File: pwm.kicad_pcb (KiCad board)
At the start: 2 copper layers, 10 parts, among them U501 LTC6992IS6-1

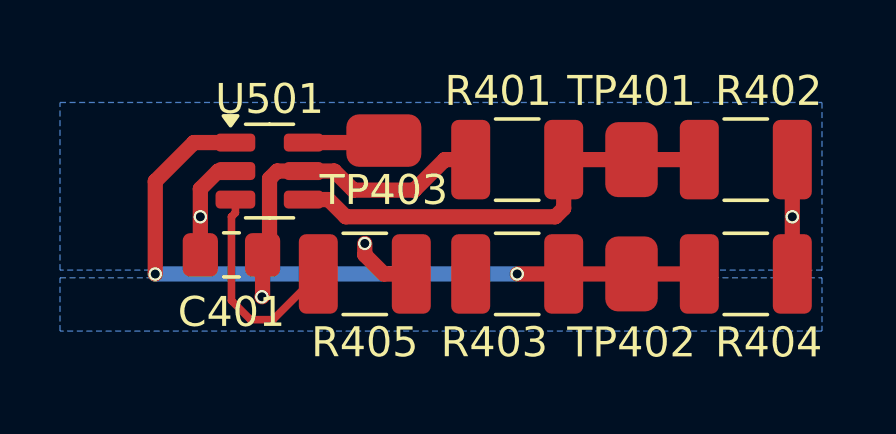
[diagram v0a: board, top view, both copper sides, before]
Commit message: enhance silk screen
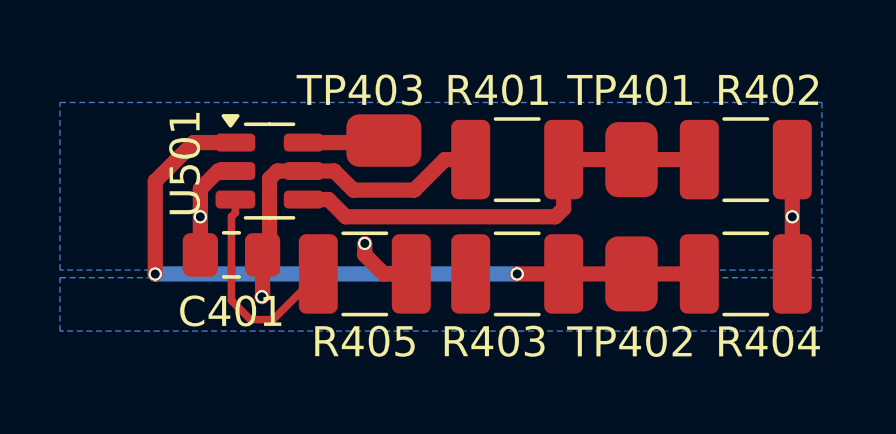
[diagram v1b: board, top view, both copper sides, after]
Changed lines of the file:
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@@
 		(tags "resistor")
 		(property "Reference" "TP403"
-			(at 0 -1.65 180)
+			(at 0.762 1.651 180)
 			(layer "F.SilkS")
 			(effects
@@
 		(tags "capacitor handsolder")
 		(property "Reference" "C401"
-			(at 0 1.905 360)
+			(at 0 1.905 0)
 			(layer "F.SilkS")
 			(effects
@@
 		)
 		(property "Value" "100n"
-			(at 0 1.68 360)
+			(at 0 1.68 0)
 			(layer "F.Fab")
 			(effects
@@
 		)
 		(fp_text user "${REFERENCE}"
-			(at 0 0 360)
+			(at 0 0 0)
 			(layer "F.Fab")
 			(effects
@@
 		)
 		(property "Value" "~"
-			(at 0 1.65 270)
+			(at 0 1.65 -90)
 			(layer "F.Fab")
 			(effects
@@
 		)
 		(fp_text user "${REFERENCE}"
-			(at 0 0 270)
+			(at 0 0 -90)
 			(layer "F.Fab")
 			(effects
@@
 		(tags "TSOT TO_SOT_SMD")
 		(property "Reference" "U501"
-			(at 0 -2.4 360)
+			(at -2.794 -0.254 90)
 			(layer "F.SilkS")
 			(effects
@@
 		)
 		(property "Value" "LTC6992IS6-1"
-			(at 2.365 6.21 360)
+			(at 2.365 6.21 0)
 			(layer "F.Fab")
 			(effects
@@
 		)
 		(fp_text user "${REFERENCE}"
-			(at 0 0 360)
-			(layer "F.Fab")
-			(effects
+			(at 0 0 0)
+			(layer "F.Fab")
+			(effects
